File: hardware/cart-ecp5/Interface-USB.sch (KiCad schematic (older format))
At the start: 40 parts, among them J5 USB_C_USB2.0, U10 93C46BT-I_OT, U11 FT2232HQ, U3 USBLC6-2SC6, X2 DSC60xx

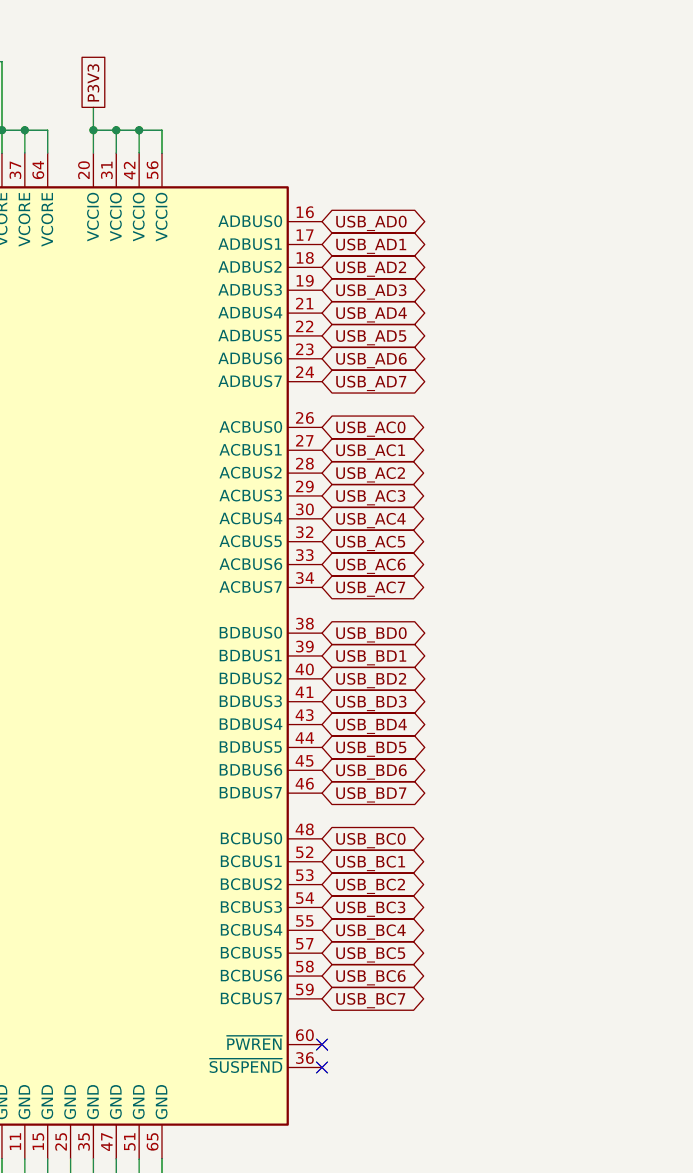
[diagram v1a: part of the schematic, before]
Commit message: Add notes on FT245 synchronous FIFO clock signal
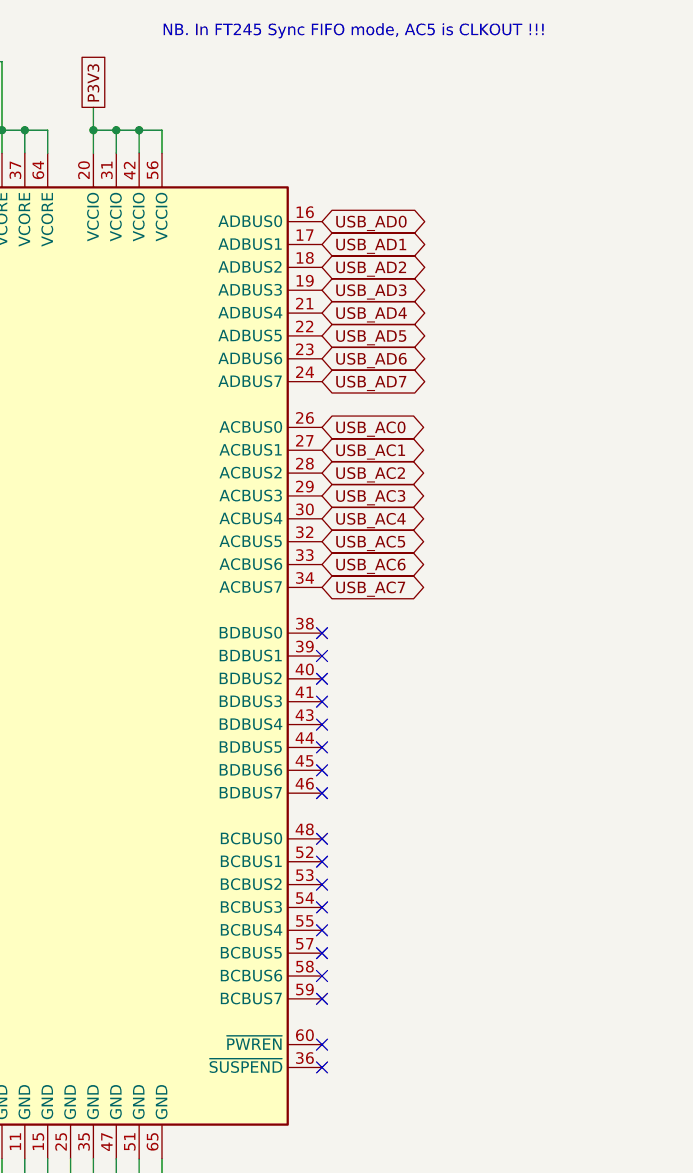
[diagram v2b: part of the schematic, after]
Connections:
- net USB_BC0: no longer names the net of U11.48 (BCBUS0)
- net USB_BC1: no longer names the net of U11.52 (BCBUS1)
- net USB_BC2: no longer names the net of U11.53 (BCBUS2)
- net USB_BC3: no longer names the net of U11.54 (BCBUS3)
- net USB_BC4: no longer names the net of U11.55 (BCBUS4)
- net USB_BC5: no longer names the net of U11.57 (BCBUS5)
- net USB_BC6: no longer names the net of U11.58 (BCBUS6)
- net USB_BC7: no longer names the net of U11.59 (BCBUS7)
- net USB_BD0: no longer names the net of U11.38 (BDBUS0)
- net USB_BD1: no longer names the net of U11.39 (BDBUS1)
- net USB_BD2: no longer names the net of U11.40 (BDBUS2)
- net USB_BD3: no longer names the net of U11.41 (BDBUS3)
- net USB_BD4: no longer names the net of U11.43 (BDBUS4)
- net USB_BD5: no longer names the net of U11.44 (BDBUS5)
- net USB_BD6: no longer names the net of U11.45 (BDBUS6)
- net USB_BD7: no longer names the net of U11.46 (BDBUS7)
- no-connect marks 5 -> 21
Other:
- note added: "NB. In FT245 Sync FIFO mode, AC5 is CLKOUT !!!"
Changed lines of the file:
@@
 Wire Wire Line
 	6250 4550 7450 4550
-Text GLabel 9950 3550 2    50   BiDi ~ 0
-USB_BD0
-Text GLabel 9950 3650 2    50   BiDi ~ 0
-USB_BD1
-Text GLabel 9950 3750 2    50   BiDi ~ 0
-USB_BD2
-Text GLabel 9950 3850 2    50   BiDi ~ 0
-USB_BD3
-Text GLabel 9950 3950 2    50   BiDi ~ 0
-USB_BD4
-Text GLabel 9950 4050 2    50   BiDi ~ 0
-USB_BD5
-Text GLabel 9950 4150 2    50   BiDi ~ 0
-USB_BD6
-Text GLabel 9950 4250 2    50   BiDi ~ 0
-USB_BD7
-Text GLabel 9950 4450 2    50   BiDi ~ 0
-USB_BC0
-Text GLabel 9950 4550 2    50   BiDi ~ 0
-USB_BC1
-Text GLabel 9950 4650 2    50   BiDi ~ 0
-USB_BC2
-Text GLabel 9950 4750 2    50   BiDi ~ 0
-USB_BC3
-Text GLabel 9950 4850 2    50   BiDi ~ 0
-USB_BC4
-Text GLabel 9950 4950 2    50   BiDi ~ 0
-USB_BC5
-Text GLabel 9950 5050 2    50   BiDi ~ 0
-USB_BC6
-Text GLabel 9950 5150 2    50   BiDi ~ 0
-USB_BC7
 $Comp
 L Device:R R?
@@
 Text Label 2400 6000 0    50   ~ 0
 USB_VPLL
+NoConn ~ 9950 3550
+NoConn ~ 9950 3650
+NoConn ~ 9950 3750
+NoConn ~ 9950 3850
+NoConn ~ 9950 3950
+NoConn ~ 9950 4050
+NoConn ~ 9950 4150
+NoConn ~ 9950 4250
+NoConn ~ 9950 4450
+NoConn ~ 9950 4550
+NoConn ~ 9950 4650
+NoConn ~ 9950 4750
+NoConn ~ 9950 4850
+NoConn ~ 9950 4950
+NoConn ~ 9950 5050
+NoConn ~ 9950 5150
+Text Notes 9250 950  0    50   ~ 0
+NB. In FT245 Sync FIFO mode, AC5 is CLKOUT !!!
 $EndSCHEMATC

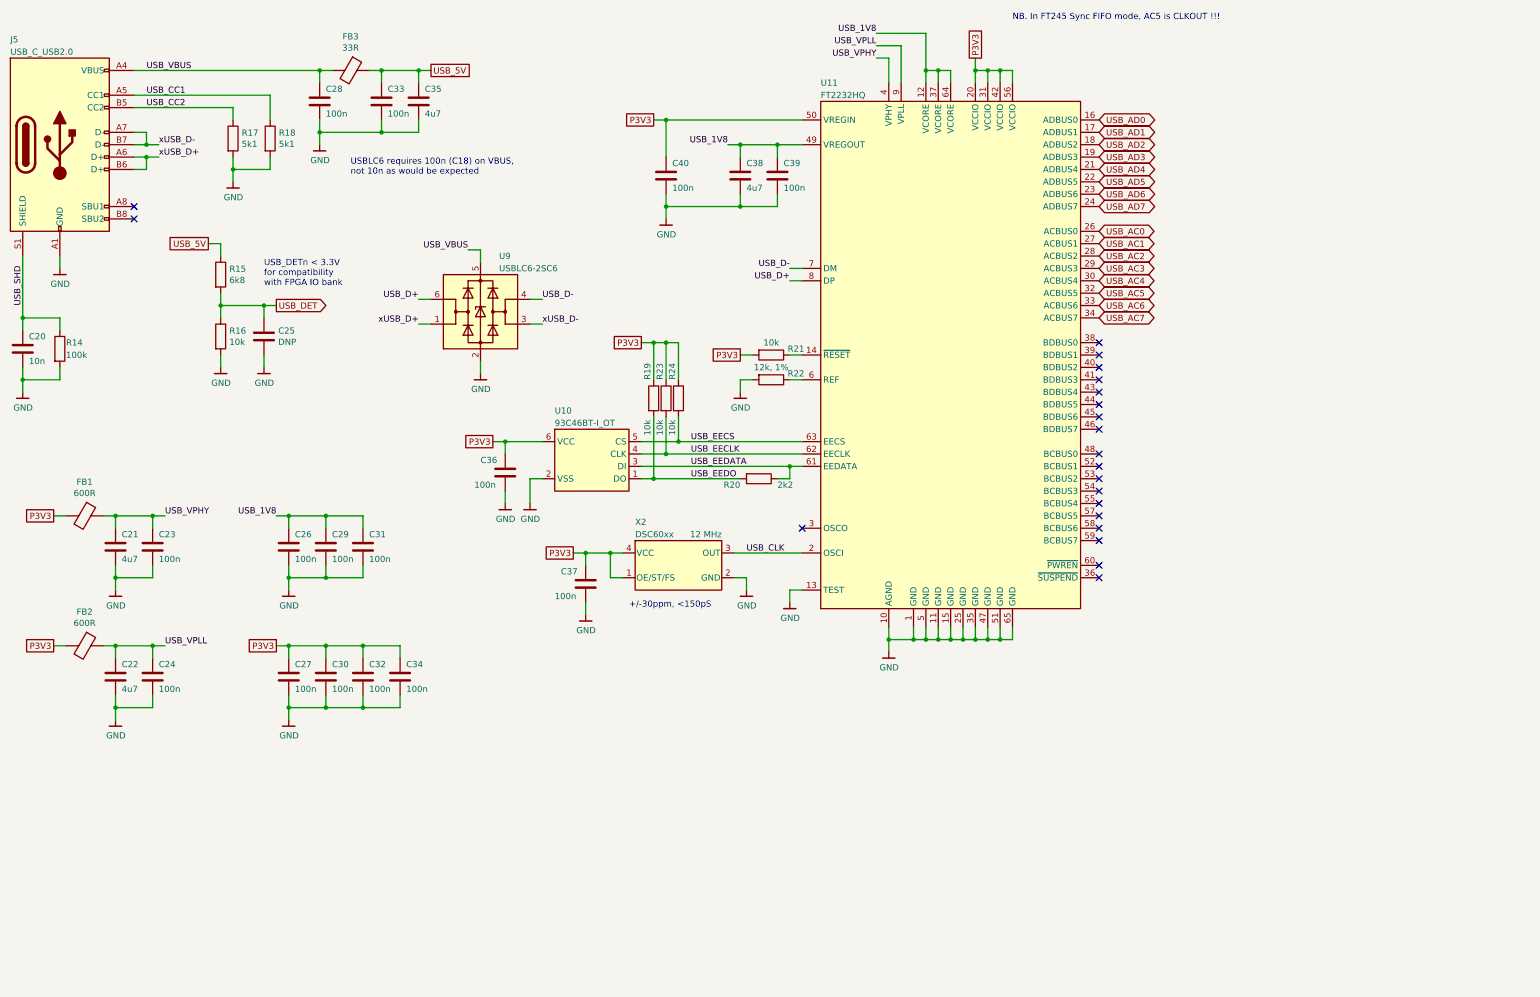
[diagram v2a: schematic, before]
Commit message: USB interface schematic cleanup
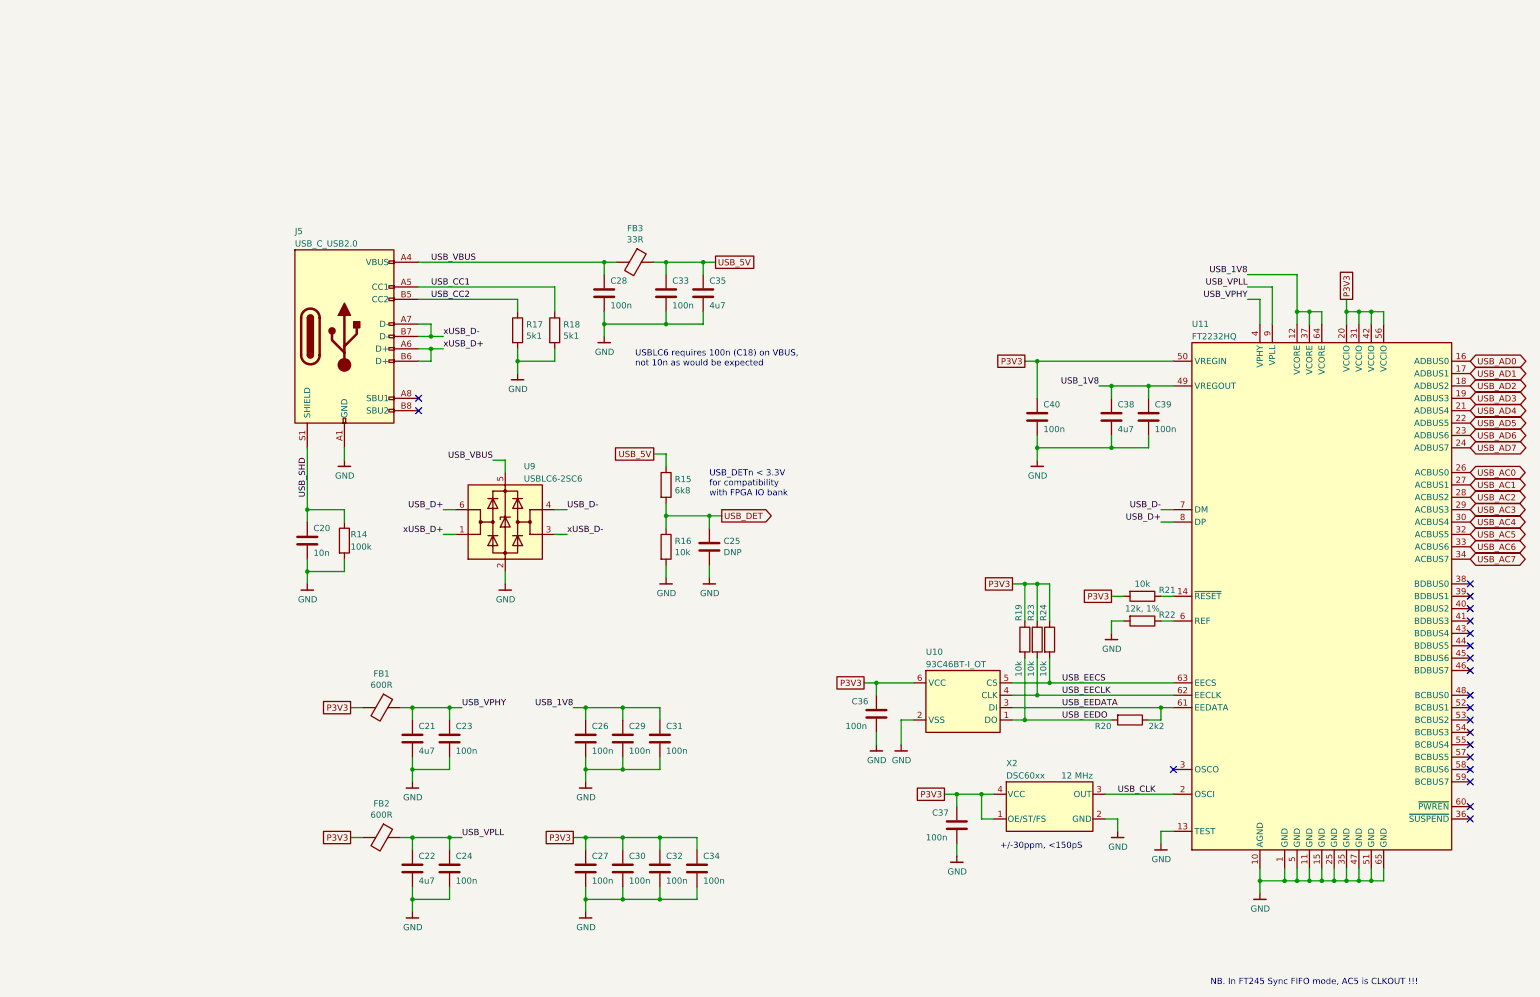
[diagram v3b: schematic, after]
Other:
- moved on the sheet: C20, C21, C22, C23, C24, C25, C26, C27, C28, C29, C30, C31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

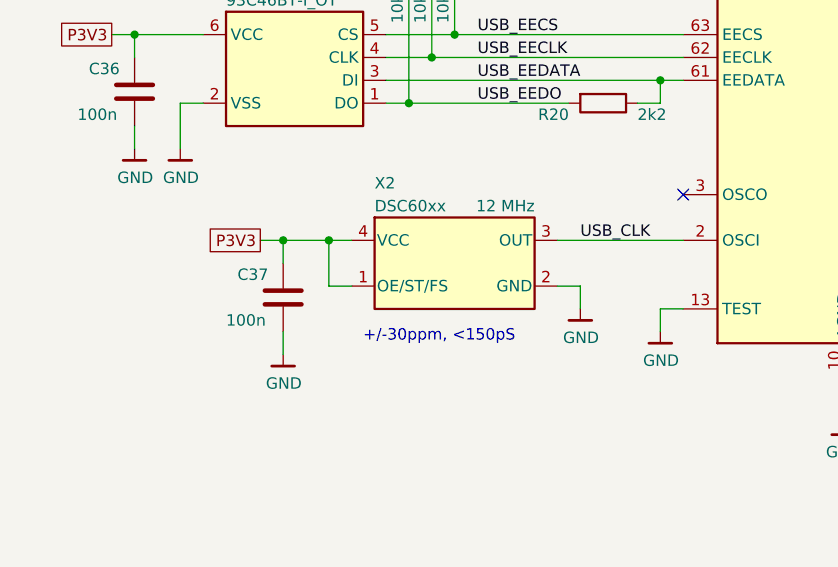
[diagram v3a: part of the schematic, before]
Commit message: Add testpoints for clock oscillator outputs
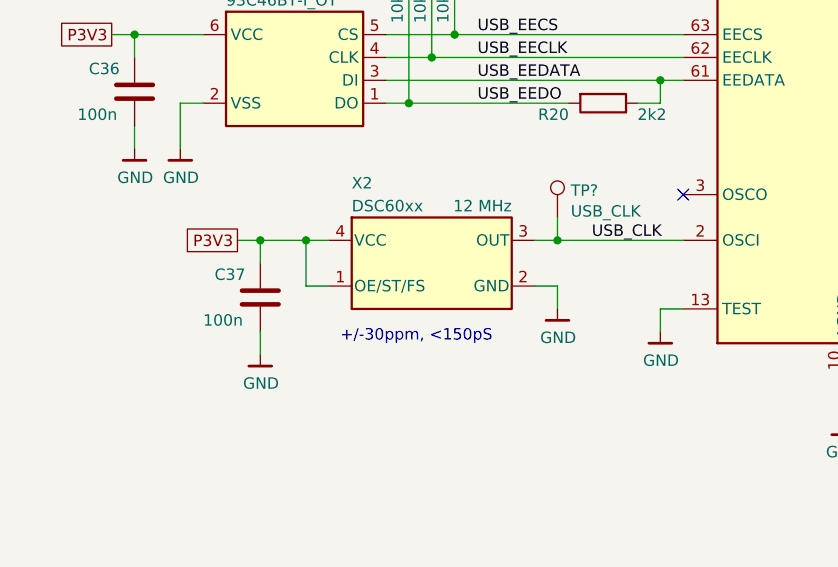
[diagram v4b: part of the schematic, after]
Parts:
- added TP?: USB_CLK, symbol Connector:TestPoint
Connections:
- net USB_CLK: now also TP?.1
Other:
- moved on the sheet: C37, X2
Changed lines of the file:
@@
 L ng_osc:DSC60xx X2
 U 1 1 5F1F4760
-P 9550 7300
-F 0 "X2" H 9200 7650 50  0000 L CNN
-F 1 "DSC60xx" H 9200 7550 50  0000 L CNN
-F 2 "ng_time:Oscillator_2.5x2.0" H 10250 6950 50  0001 C CNN
-F 3 "" H 9450 7300 50  0001 C CNN
-F 4 "12 MHz" H 9900 7550 50  0000 R CNN "Freq"
-	1    9550 7300
-	1    0    0    -1
-$EndComp
-Wire Wire Line
-	10000 7200 10550 7200
-Wire Wire Line
-	10000 7400 10100 7400
-Wire Wire Line
-	10100 7400 10100 7500
+P 9450 7300
+F 0 "X2" H 9100 7650 50  0000 L CNN
+F 1 "DSC60xx" H 9100 7550 50  0000 L CNN
+F 2 "ng_time:Oscillator_2.5x2.0" H 10150 6950 50  0001 C CNN
+F 3 "" H 9350 7300 50  0001 C CNN
+F 4 "12 MHz" H 9800 7550 50  0000 R CNN "Freq"
+	1    9450 7300
+	1    0    0    -1
+$EndComp
+Wire Wire Line
+	9900 7200 10000 7200
+Wire Wire Line
+	9900 7400 10000 7400
+Wire Wire Line
+	10000 7400 10000 7500
 $Comp
 L Device:C C37
 U 1 1 5F1F476F
-P 8800 7450
-F 0 "C37" H 8600 7550 50  0000 L CNN
-F 1 "100n" H 8550 7350 50  0000 L CNN
-F 2 "Capacitor_SMD:C_0402_1005Metric" H 8838 7300 50  0001 C CNN
-F 3 "~" H 8800 7450 50  0001 C CNN
-	1    8800 7450
-	1    0    0    -1
-$EndComp
-Wire Wire Line
-	8800 7600 8800 7700
-Wire Wire Line
-	9100 7400 9000 7400
-Wire Wire Line
-	9000 7400 9000 7200
-Wire Wire Line
-	9000 7200 9100 7200
+P 8700 7450
+F 0 "C37" H 8500 7550 50  0000 L CNN
+F 1 "100n" H 8450 7350 50  0000 L CNN
+F 2 "Capacitor_SMD:C_0402_1005Metric" H 8738 7300 50  0001 C CNN
+F 3 "~" H 8700 7450 50  0001 C CNN
+	1    8700 7450
+	1    0    0    -1
+$EndComp
+Wire Wire Line
+	8700 7600 8700 7700
+Wire Wire Line
+	9000 7400 8900 7400
+Wire Wire Line
+	8900 7400 8900 7200
+Wire Wire Line
+	8900 7200 9000 7200
 Wire Wire Line
 	10050 4400 10350 4400
@@
 	8150 6300 8150 6400
 Wire Wire Line
-	9000 7200 8800 7200
-Connection ~ 9000 7200
-Wire Wire Line
-	8800 7200 8800 7300
+	8900 7200 8700 7200
+Connection ~ 8900 7200
+Wire Wire Line
+	8700 7200 8700 7300
 $Comp
 L Device:C C21
@@
 L ng_power:GND #PWR0115
 U 1 1 5F44F292
-P 10100 7500
+P 10000 7500
 AR Path="/5F44F292" Ref="#PWR0115"  Part="1"
 AR Path="/5F302051/5F44F292" Ref="#PWR?"  Part="1"
 AR Path="/5F4552C5/5F44F292" Ref="#PWR045"  Part="1"
-F 0 "#PWR045" H 10100 7250 50  0001 C CNN
-F 1 "GND" H 10103 7374 50  0000 C CNN
-F 2 "" H 10000 7150 50  0001 C CNN
-F 3 "" H 10100 7500 50  0001 C CNN
-	1    10100 7500
+F 0 "#PWR045" H 10000 7250 50  0001 C CNN
+F 1 "GND" H 10003 7374 50  0000 C CNN
+F 2 "" H 9900 7150 50  0001 C CNN
+F 3 "" H 10000 7500 50  0001 C CNN
+	1    10000 7500
 	1    0    0    -1
 $EndComp
@@
 L ng_power:GND #PWR0116
 U 1 1 5F44F69A
-P 8800 7700
+P 8700 7700
 AR Path="/5F44F69A" Ref="#PWR0116"  Part="1"
 AR Path="/5F302051/5F44F69A" Ref="#PWR?"  Part="1"
 AR Path="/5F4552C5/5F44F69A" Ref="#PWR043"  Part="1"
-F 0 "#PWR043" H 8800 7450 50  0001 C CNN
-F 1 "GND" H 8803 7574 50  0000 C CNN
-F 2 "" H 8700 7350 50  0001 C CNN
-F 3 "" H 8800 7700 50  0001 C CNN
-	1    8800 7700
+F 0 "#PWR043" H 8700 7450 50  0001 C CNN
+F 1 "GND" H 8703 7574 50  0000 C CNN
+F 2 "" H 8600 7350 50  0001 C CNN
+F 3 "" H 8700 7700 50  0001 C CNN
+	1    8700 7700
 	1    0    0    -1
 $EndComp
@@
 P3V3
 Wire Wire Line
-	8800 7200 8700 7200
-Text GLabel 8700 7200 0    50   UnSpc ~ 0
+	8700 7200 8600 7200
+Text GLabel 8600 7200 0    50   UnSpc ~ 0
 P3V3
 Text GLabel 10050 5600 0    50   UnSpc ~ 0
@@
 Text GLabel 11950 3200 1    50   UnSpc ~ 0
 P3V3
-Connection ~ 8800 7200
+Connection ~ 8700 7200
 Connection ~ 5800 6500
 Connection ~ 5800 7550
@@
 	0    1    1    0
 $EndComp
-Text Label 10100 7200 0    50   ~ 0
+Text Label 10150 7200 0    50   ~ 0
 USB_CLK
 Text Label 9650 6300 0    50   ~ 0
@@
 Text Label 4550 3200 0    50   ~ 0
 USB_CC2
-Text Notes 9150 7650 0    50   ~ 0
+Text Notes 9050 7650 0    50   ~ 0
 +/-30ppm, <150pS
 Text Label 4650 5100 2    50   ~ 0
@@
 Text Notes 10850 8750 0    50   ~ 0
 NB. In FT245 Sync FIFO mode, AC5 is CLKOUT !!!
+Wire Wire Line
+	10000 7200 10000 7100
+$Comp
+L Connector:TestPoint TP?
+U 1 1 5FE0424B
+P 10000 7100
+AR Path="/5F483803/5FE0424B" Ref="TP?"  Part="1"
+AR Path="/5F3E46DE/5FE0424B" Ref="TP?"  Part="1"
+AR Path="/5F4552C5/5FE0424B" Ref="TP?"  Part="1"
+F 0 "TP?" H 10058 7218 50  0000 L CNN
+F 1 "USB_CLK" H 10058 7127 50  0000 L CNN
+F 2 "" H 10200 7100 50  0001 C CNN
+F 3 "~" H 10200 7100 50  0001 C CNN
+	1    10000 7100
+	1    0    0    -1
+$EndComp
+Connection ~ 10000 7200
+Wire Wire Line
+	10000 7200 10550 7200
 $EndSCHEMATC

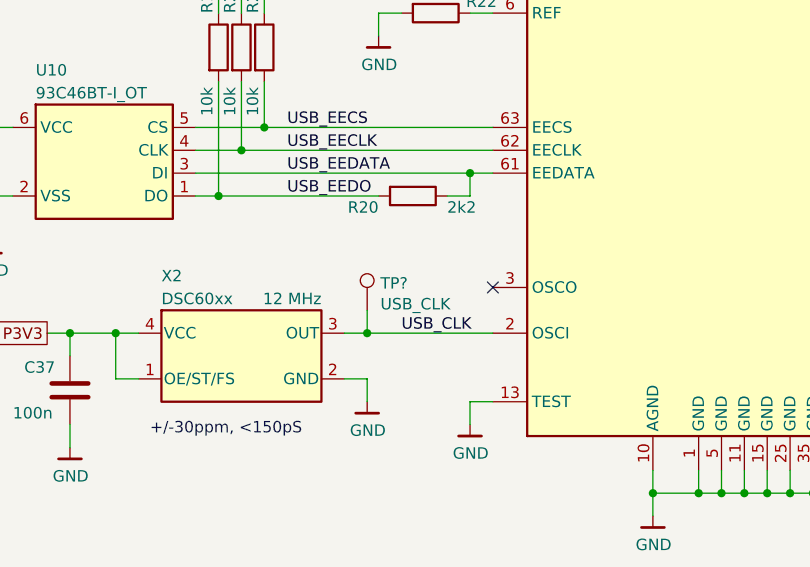
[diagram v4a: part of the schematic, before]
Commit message: Layout testpoints for power rails and clock oscillators
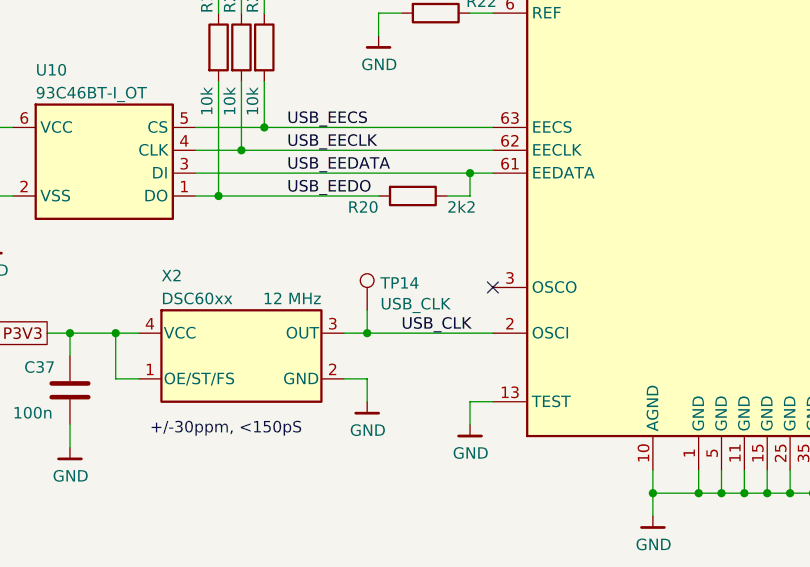
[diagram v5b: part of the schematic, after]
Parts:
- TP14: renamed from TP?; footprint (none) -> ng_test:TestPoint_Pad_D0.5mm
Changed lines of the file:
@@
 AR Path="/5F483803/5FE0424B" Ref="TP?"  Part="1"
 AR Path="/5F3E46DE/5FE0424B" Ref="TP?"  Part="1"
-AR Path="/5F4552C5/5FE0424B" Ref="TP?"  Part="1"
-F 0 "TP?" H 10058 7218 50  0000 L CNN
+AR Path="/5F4552C5/5FE0424B" Ref="TP14"  Part="1"
+F 0 "TP14" H 10058 7218 50  0000 L CNN
 F 1 "USB_CLK" H 10058 7127 50  0000 L CNN
-F 2 "" H 10200 7100 50  0001 C CNN
+F 2 "ng_test:TestPoint_Pad_D0.5mm" H 10200 7100 50  0001 C CNN
 F 3 "~" H 10200 7100 50  0001 C CNN
 	1    10000 7100

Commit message: Use 0402 package for all 4u7 bypass capacitors
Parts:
- C38, C5: footprint Capacitor_SMD:C_0603_1608Metric -> Capacitor_SMD:C_0402_1005Metric
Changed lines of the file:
@@
 F 0 "C38" H 10000 4250 50  0000 R CNN
 F 1 "4u7" H 10000 4050 50  0000 R CNN
-F 2 "Capacitor_SMD:C_0603_1608Metric" H 10088 4000 50  0001 C CNN
+F 2 "Capacitor_SMD:C_0402_1005Metric" H 10088 4000 50  0001 C CNN
 F 3 "~" H 10050 4150 50  0001 C CNN
 	1    10050 4150
@@
 F 0 "C35" H 6800 3250 50  0000 L CNN
 F 1 "4u7" H 6800 3050 50  0000 L CNN
-F 2 "Capacitor_SMD:C_0603_1608Metric" H 6788 3000 50  0001 C CNN
+F 2 "Capacitor_SMD:C_0402_1005Metric" H 6788 3000 50  0001 C CNN
 F 3 "~" H 6750 3150 50  0001 C CNN
 F 4 "" H 6750 3150 50  0001 C CNN "MPN"

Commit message: Finish converting 4u7 caps to 0402
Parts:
- C21, C22: footprint Capacitor_SMD:C_0603_1608Metric -> Capacitor_SMD:C_0402_1005Metric
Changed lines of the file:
@@
 F 0 "C21" H 4450 6850 50  0000 L CNN
 F 1 "4u7" H 4450 6650 50  0000 L CNN
-F 2 "Capacitor_SMD:C_0603_1608Metric" H 4438 6600 50  0001 C CNN
+F 2 "Capacitor_SMD:C_0402_1005Metric" H 4438 6600 50  0001 C CNN
 F 3 "~" H 4400 6750 50  0001 C CNN
 	1    4400 6750
@@
 F 0 "C22" H 4450 7900 50  0000 L CNN
 F 1 "4u7" H 4450 7700 50  0000 L CNN
-F 2 "Capacitor_SMD:C_0603_1608Metric" H 4438 7650 50  0001 C CNN
+F 2 "Capacitor_SMD:C_0402_1005Metric" H 4438 7650 50  0001 C CNN
 F 3 "~" H 4400 7800 50  0001 C CNN
 	1    4400 7800
